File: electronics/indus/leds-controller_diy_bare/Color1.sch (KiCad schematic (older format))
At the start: 19 parts, among them Q3 Q_NPN_BCE, U4 TPS92513

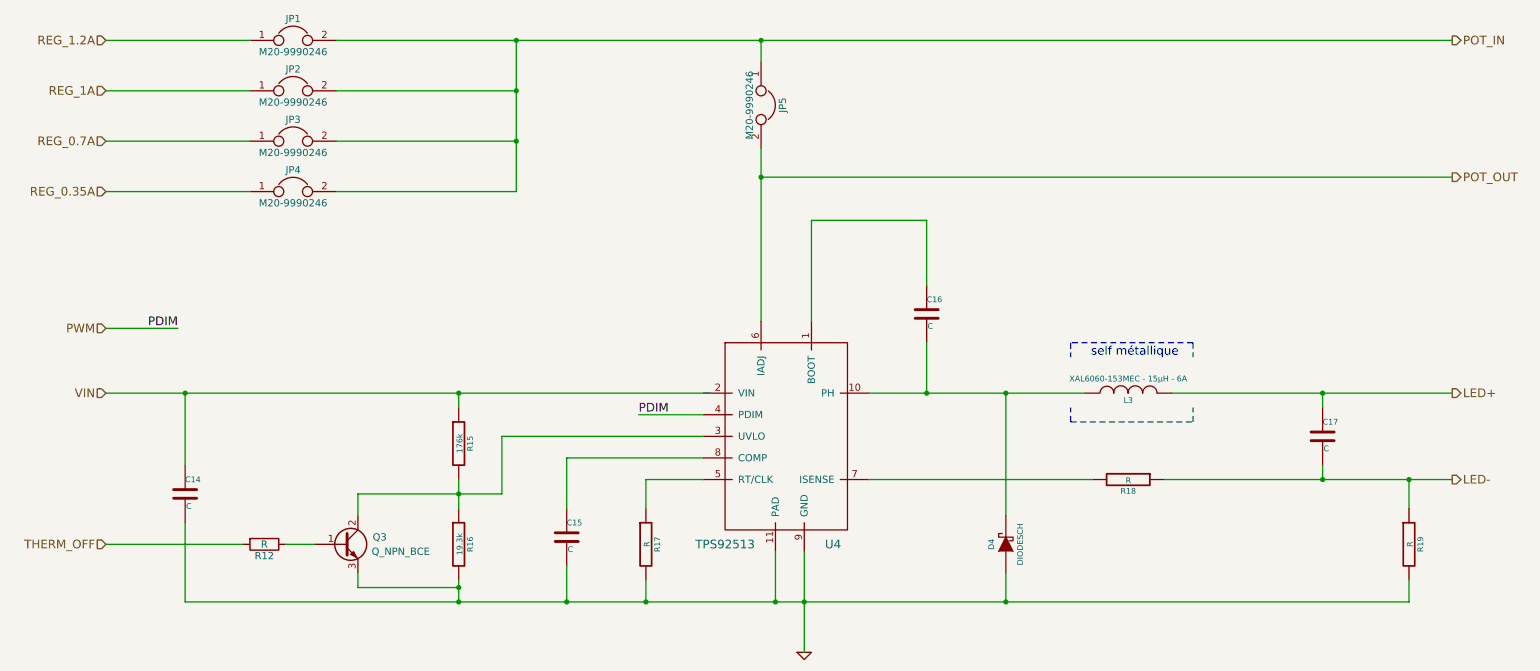
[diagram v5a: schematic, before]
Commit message: simpler schematics with a lot of values now
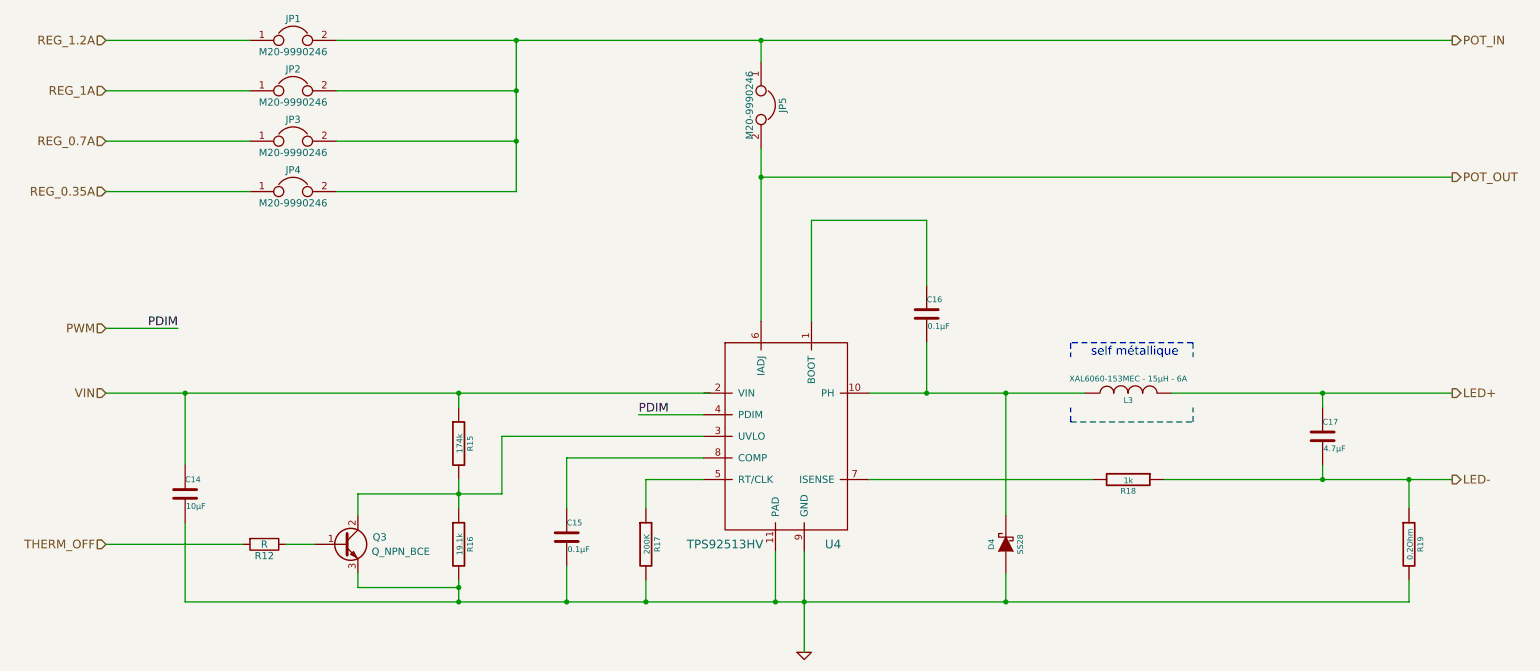
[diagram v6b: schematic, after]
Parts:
- C14: value C -> 10µF
- C15, C16: value C -> 0.1µF
- C17: value C -> 4.7µF
- D4: value DIODESCH -> SS28
- R15: value 176k -> 174k
- R16: value 19.3k -> 19.1k
- R17: value R -> 200K
- R18: value R -> 1k
- R19: value R -> 0.2Ohm
- U4: value TPS92513 -> TPS92513HV
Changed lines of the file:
@@
 P 5800 3550
 F 0 "U4" H 6150 2600 60  0000 C CNN
-F 1 "TPS92513" H 5400 2600 60  0000 C CNN
+F 1 "TPS92513HV" H 5400 2600 60  0000 C CNN
 F 2 "" H 5950 3650 60  0000 C CNN
 F 3 "" H 5950 3650 60  0000 C CNN
@@
 P 1650 4150
 F 0 "C14" H 1650 4250 40  0000 L CNN
-F 1 "C" H 1656 4065 40  0000 L CNN
+F 1 "10µF" H 1656 4065 40  0000 L CNN
 F 2 "" H 1688 4000 30  0000 C CNN
 F 3 "" H 1650 4150 60  0000 C CNN
@@
 P 3550 3800
 F 0 "R15" V 3630 3800 40  0000 C CNN
-F 1 "176k" V 3557 3801 40  0000 C CNN
+F 1 "174k" V 3557 3801 40  0000 C CNN
 F 2 "" V 3480 3800 30  0000 C CNN
 F 3 "" H 3550 3800 30  0000 C CNN
@@
 P 3550 4500
 F 0 "R16" V 3630 4500 40  0000 C CNN
-F 1 "19.3k" V 3557 4501 40  0000 C CNN
+F 1 "19.1k" V 3557 4501 40  0000 C CNN
 F 2 "" V 3480 4500 30  0000 C CNN
 F 3 "" H 3550 4500 30  0000 C CNN
@@
 P 4300 4450
 F 0 "C15" H 4300 4550 40  0000 L CNN
-F 1 "C" H 4306 4365 40  0000 L CNN
+F 1 "0.1µF" H 4306 4365 40  0000 L CNN
 F 2 "" H 4338 4300 30  0000 C CNN
 F 3 "" H 4300 4450 60  0000 C CNN
@@
 P 4850 4500
 F 0 "R17" V 4930 4500 40  0000 C CNN
-F 1 "R" V 4857 4501 40  0000 C CNN
+F 1 "200K" V 4857 4501 40  0000 C CNN
 F 2 "" V 4780 4500 30  0000 C CNN
 F 3 "" H 4850 4500 30  0000 C CNN
@@
 P 6800 2900
 F 0 "C16" H 6800 3000 40  0000 L CNN
-F 1 "C" H 6806 2815 40  0000 L CNN
+F 1 "0.1µF" H 6806 2815 40  0000 L CNN
 F 2 "" H 6838 2750 30  0000 C CNN
 F 3 "" H 6800 2900 60  0000 C CNN
@@
 P 9550 3750
 F 0 "C17" H 9550 3850 40  0000 L CNN
-F 1 "C" H 9556 3665 40  0000 L CNN
+F 1 "4.7µF" H 9556 3665 40  0000 L CNN
 F 2 "" H 9588 3600 30  0000 C CNN
 F 3 "" H 9550 3750 60  0000 C CNN
@@
 P 8200 4050
 F 0 "R18" V 8280 4050 40  0000 C CNN
-F 1 "R" V 8207 4051 40  0000 C CNN
+F 1 "1k" V 8207 4051 40  0000 C CNN
 F 2 "" V 8130 4050 30  0000 C CNN
 F 3 "" H 8200 4050 30  0000 C CNN
@@
 P 10150 4500
 F 0 "R19" V 10230 4500 40  0000 C CNN
-F 1 "R" V 10157 4501 40  0000 C CNN
+F 1 "0.2Ohm" V 10157 4501 40  0000 C CNN
 F 2 "" V 10080 4500 30  0000 C CNN
 F 3 "" H 10150 4500 30  0000 C CNN
@@
 P 7350 4500
 F 0 "D4" H 7350 4600 40  0000 C CNN
-F 1 "DIODESCH" H 7350 4400 40  0000 C CNN
+F 1 "SS28" H 7350 4400 40  0000 C CNN
 F 2 "" H 7350 4500 60  0000 C CNN
 F 3 "" H 7350 4500 60  0000 C CNN

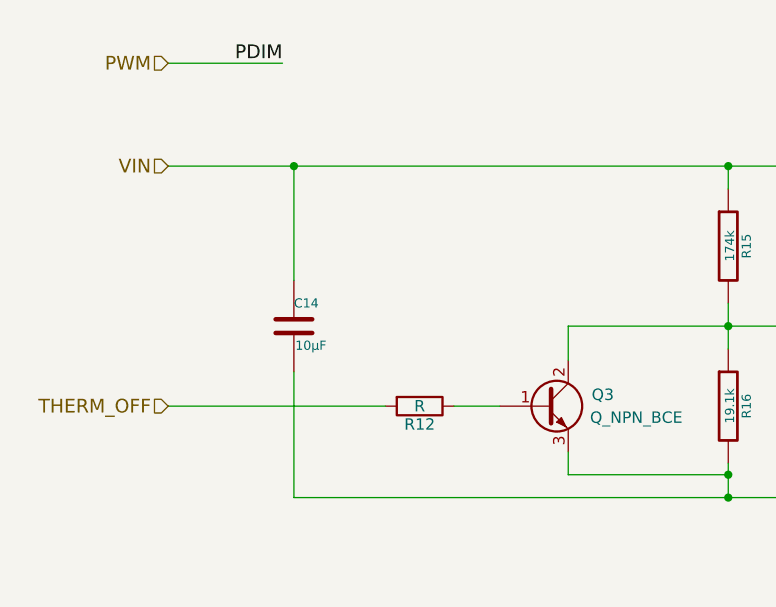
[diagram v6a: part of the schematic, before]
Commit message: Added missing Capa & Resistor values
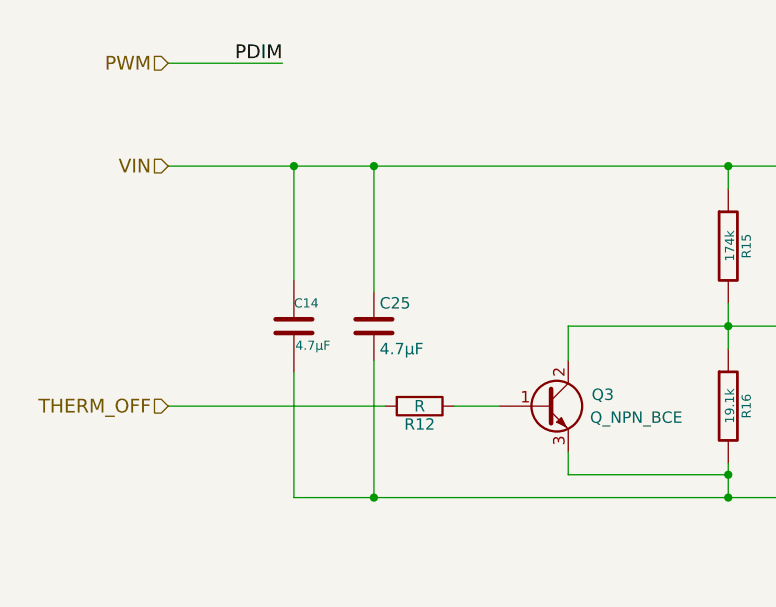
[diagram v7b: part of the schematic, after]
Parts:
- added C25: 4.7µF, symbol C
- C14: value 10µF -> 4.7µF
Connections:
- net GND: now also C25.2
- net VIN: now also C25.1
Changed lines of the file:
@@
 P 1650 4150
 F 0 "C14" H 1650 4250 40  0000 L CNN
-F 1 "10µF" H 1656 4065 40  0000 L CNN
+F 1 "4.7µF" H 1656 4065 40  0000 L CNN
 F 2 "" H 1688 4000 30  0000 C CNN
 F 3 "" H 1650 4150 60  0000 C CNN
@@
 Wire Wire Line
 	2050 4500 1100 4500
+$Comp
+L C C25
+U 1 1 576AC3F8
+P 2000 4150
+F 0 "C25" H 2025 4250 50  0000 L CNN
+F 1 "4.7µF" H 2025 4050 50  0000 L CNN
+F 2 "" H 2038 4000 50  0000 C CNN
+F 3 "" H 2000 4150 50  0000 C CNN
+	1    2000 4150
+	1    0    0    -1
+$EndComp
+Wire Wire Line
+	2000 4000 2000 3450
+Connection ~ 2000 3450
+Wire Wire Line
+	2000 4300 2000 4900
+Connection ~ 2000 4900
 $EndSCHEMATC

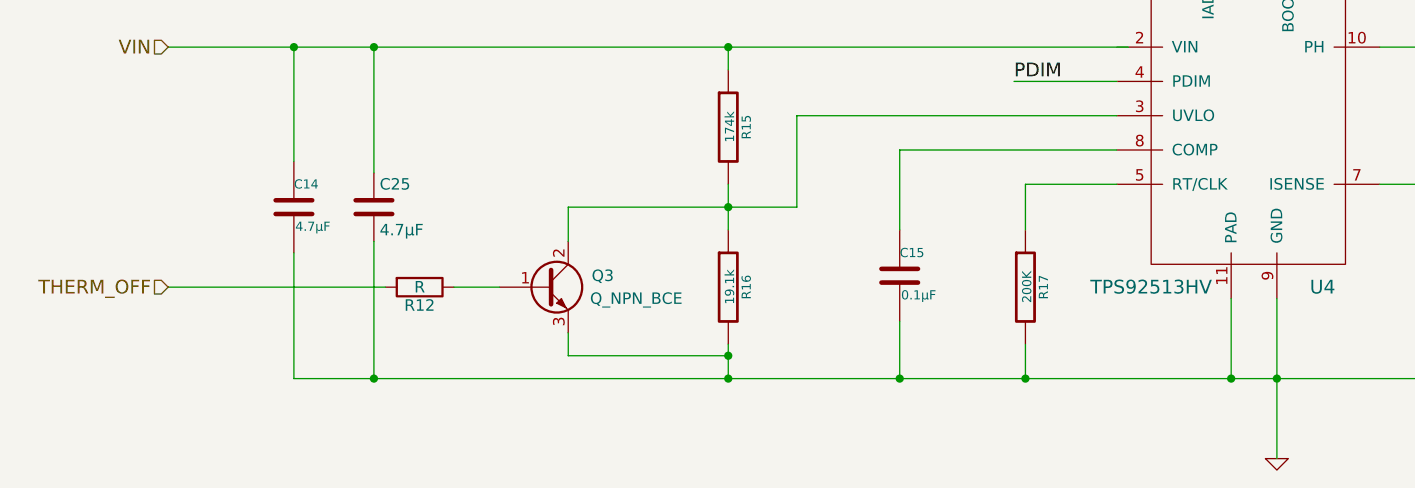
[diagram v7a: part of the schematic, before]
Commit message: footprint with libraries
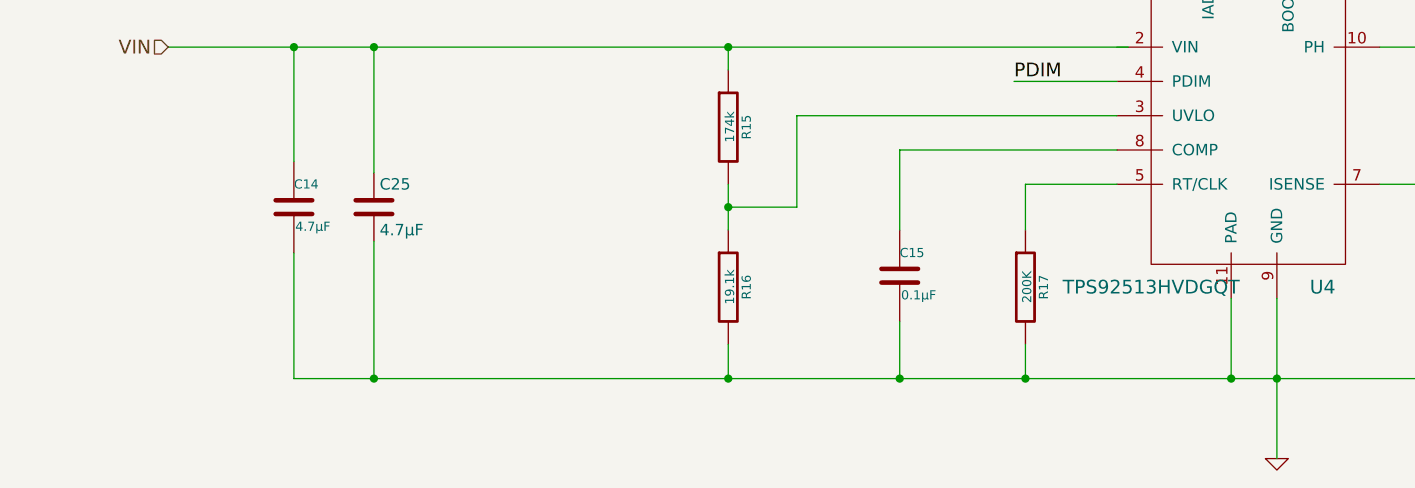
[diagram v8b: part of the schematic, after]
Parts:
- removed Q3: Q_NPN_BCE, symbol Q_NPN_BCE
- removed R12: R, symbol R
- C14, C17, C25: footprint (none) -> Capacitors_SMD:C_1206
- C15, C16: footprint (none) -> Capacitors_SMD:C_0805
- D4: footprint (none) -> Diodes_SMD:SOD-123
- R15, R16, R17, R18: footprint (none) -> Resistors_SMD:R_0805
- R19: footprint (none) -> Resistors_SMD:R_1206
- U4: value TPS92513HV -> TPS92513HVDGQT; footprint (none) -> risebox:BUCK_TPS92513_PowerPAD
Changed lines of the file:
@@
 P 5800 3550
 F 0 "U4" H 6150 2600 60  0000 C CNN
-F 1 "TPS92513HV" H 5400 2600 60  0000 C CNN
-F 2 "" H 5950 3650 60  0000 C CNN
+F 1 "TPS92513HVDGQT" H 5400 2600 60  0000 C CNN
+F 2 "risebox:BUCK_TPS92513_PowerPAD" H 5950 3650 60  0001 C CNN
 F 3 "" H 5950 3650 60  0000 C CNN
 	1    5800 3550
@@
 F 0 "C14" H 1650 4250 40  0000 L CNN
 F 1 "4.7µF" H 1656 4065 40  0000 L CNN
-F 2 "" H 1688 4000 30  0000 C CNN
+F 2 "Capacitors_SMD:C_1206" H 1688 4000 30  0001 C CNN
 F 3 "" H 1650 4150 60  0000 C CNN
 	1    1650 4150
@@
 $EndComp
 $Comp
-L GND-RESCUE-leds-controller #PWR12
+L GND-RESCUE-leds-controller #PWR013
 U 1 1 571557B2
 P 5950 5250
-F 0 "#PWR12" H 5950 5250 30  0001 C CNN
+F 0 "#PWR013" H 5950 5250 30  0001 C CNN
 F 1 "GND" H 5950 5180 30  0001 C CNN
 F 2 "" H 5950 5250 60  0000 C CNN
@@
 F 0 "R15" V 3630 3800 40  0000 C CNN
 F 1 "174k" V 3557 3801 40  0000 C CNN
-F 2 "" V 3480 3800 30  0000 C CNN
+F 2 "Resistors_SMD:R_0805" V 3480 3800 30  0001 C CNN
 F 3 "" H 3550 3800 30  0000 C CNN
 	1    3550 3800
@@
 F 0 "R16" V 3630 4500 40  0000 C CNN
 F 1 "19.1k" V 3557 4501 40  0000 C CNN
-F 2 "" V 3480 4500 30  0000 C CNN
+F 2 "Resistors_SMD:R_0805" V 3480 4500 30  0001 C CNN
 F 3 "" H 3550 4500 30  0000 C CNN
 	1    3550 4500
@@
 F 0 "C15" H 4300 4550 40  0000 L CNN
 F 1 "0.1µF" H 4306 4365 40  0000 L CNN
-F 2 "" H 4338 4300 30  0000 C CNN
+F 2 "Capacitors_SMD:C_0805" H 4338 4300 30  0001 C CNN
 F 3 "" H 4300 4450 60  0000 C CNN
 	1    4300 4450
@@
 F 0 "R17" V 4930 4500 40  0000 C CNN
 F 1 "200K" V 4857 4501 40  0000 C CNN
-F 2 "" V 4780 4500 30  0000 C CNN
+F 2 "Resistors_SMD:R_0805" V 4780 4500 30  0001 C CNN
 F 3 "" H 4850 4500 30  0000 C CNN
 	1    4850 4500
@@
 F 0 "C16" H 6800 3000 40  0000 L CNN
 F 1 "0.1µF" H 6806 2815 40  0000 L CNN
-F 2 "" H 6838 2750 30  0000 C CNN
+F 2 "Capacitors_SMD:C_0805" H 6838 2750 30  0001 C CNN
 F 3 "" H 6800 2900 60  0000 C CNN
 	1    6800 2900
@@
 F 0 "C17" H 9550 3850 40  0000 L CNN
 F 1 "4.7µF" H 9556 3665 40  0000 L CNN
-F 2 "" H 9588 3600 30  0000 C CNN
+F 2 "Capacitors_SMD:C_1206" H 9588 3600 30  0001 C CNN
 F 3 "" H 9550 3750 60  0000 C CNN
 	1    9550 3750
@@
 F 0 "R18" V 8280 4050 40  0000 C CNN
 F 1 "1k" V 8207 4051 40  0000 C CNN
-F 2 "" V 8130 4050 30  0000 C CNN
+F 2 "Resistors_SMD:R_0805" V 8130 4050 30  0001 C CNN
 F 3 "" H 8200 4050 30  0000 C CNN
 	1    8200 4050
@@
 F 0 "R19" V 10230 4500 40  0000 C CNN
 F 1 "0.2Ohm" V 10157 4501 40  0000 C CNN
-F 2 "" V 10080 4500 30  0000 C CNN
+F 2 "Resistors_SMD:R_1206" V 10080 4500 30  0001 C CNN
 F 3 "" H 10150 4500 30  0000 C CNN
 	1    10150 4500
@@
 F 0 "D4" H 7350 4600 40  0000 C CNN
 F 1 "SS28" H 7350 4400 40  0000 C CNN
-F 2 "" H 7350 4500 60  0000 C CNN
+F 2 "Diodes_SMD:SOD-123" H 7350 4500 60  0001 C CNN
 F 3 "" H 7350 4500 60  0000 C CNN
 	1    7350 4500
@@
 F 0 "JP1" H 2400 1150 50  0000 C CNN
 F 1 "M20-9990246" H 2400 920 50  0000 C CNN
-F 2 "" H 2400 1000 50  0000 C CNN
+F 2 "" H 2400 1000 50  0001 C CNN
 F 3 "" H 2400 1000 50  0000 C CNN
 	1    2400 1000
@@
 F 0 "JP2" H 2400 1500 50  0000 C CNN
 F 1 "M20-9990246" H 2400 1270 50  0000 C CNN
-F 2 "" H 2400 1350 50  0000 C CNN
+F 2 "" H 2400 1350 50  0001 C CNN
 F 3 "" H 2400 1350 50  0000 C CNN
 	1    2400 1350
@@
 F 0 "JP3" H 2400 1850 50  0000 C CNN
 F 1 "M20-9990246" H 2400 1620 50  0000 C CNN
-F 2 "" H 2400 1700 50  0000 C CNN
+F 2 "" H 2400 1700 50  0001 C CNN
 F 3 "" H 2400 1700 50  0000 C CNN
 	1    2400 1700
@@
 F 0 "JP4" H 2400 2200 50  0000 C CNN
 F 1 "M20-9990246" H 2400 1970 50  0000 C CNN
-F 2 "" H 2400 2050 50  0000 C CNN
+F 2 "" H 2400 2050 50  0001 C CNN
 F 3 "" H 2400 2050 50  0000 C CNN
 	1    2400 2050
@@
 F 0 "JP5" H 5650 1600 50  0000 C CNN
 F 1 "M20-9990246" H 5650 1370 50  0000 C CNN
-F 2 "" H 5650 1450 50  0000 C CNN
+F 2 "" H 5650 1450 50  0001 C CNN
 F 3 "" H 5650 1450 50  0000 C CNN
 	1    5650 1450
@@
 Connection ~ 3550 4900
 Wire Wire Line
-	2850 4300 2850 4150
-Wire Wire Line
-	2850 4150 3850 4150
-Wire Wire Line
-	2850 4700 2850 4800
-Wire Wire Line
-	2850 4800 3550 4800
-Connection ~ 3550 4800
-$Comp
-L Q_NPN_BCE Q3
-U 1 1 5763D1F6
-P 2750 4500
-F 0 "Q3" H 3050 4550 50  0000 R CNN
-F 1 "Q_NPN_BCE" H 3350 4450 50  0000 R CNN
-F 2 "" H 2950 4600 50  0000 C CNN
-F 3 "" H 2750 4500 50  0000 C CNN
-	1    2750 4500
-	1    0    0    -1
-$EndComp
-Text HLabel 1100 4500 0    60   Input ~ 0
-THERM_OFF
-$Comp
-L R R12
-U 1 1 5763D8FD
-P 2200 4500
-F 0 "R12" V 2280 4500 50  0000 C CNN
-F 1 "R" V 2200 4500 50  0000 C CNN
-F 2 "" V 2130 4500 50  0000 C CNN
-F 3 "" H 2200 4500 50  0000 C CNN
-	1    2200 4500
-	0    1    1    0
-$EndComp
-Wire Wire Line
-	2350 4500 2550 4500
-Wire Wire Line
-	2050 4500 1100 4500
+	3550 4150 3850 4150
 $Comp
 L C C25
@@
 F 0 "C25" H 2025 4250 50  0000 L CNN
 F 1 "4.7µF" H 2025 4050 50  0000 L CNN
-F 2 "" H 2038 4000 50  0000 C CNN
+F 2 "Capacitors_SMD:C_1206" H 2038 4000 50  0001 C CNN
 F 3 "" H 2000 4150 50  0000 C CNN
 	1    2000 4150
